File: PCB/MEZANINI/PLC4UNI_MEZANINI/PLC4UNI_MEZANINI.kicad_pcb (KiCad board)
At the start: 4 copper layers, 30.3 x 37.8 mm, 24 parts, among them U1 MC-121-L119, U2 MT9700-N

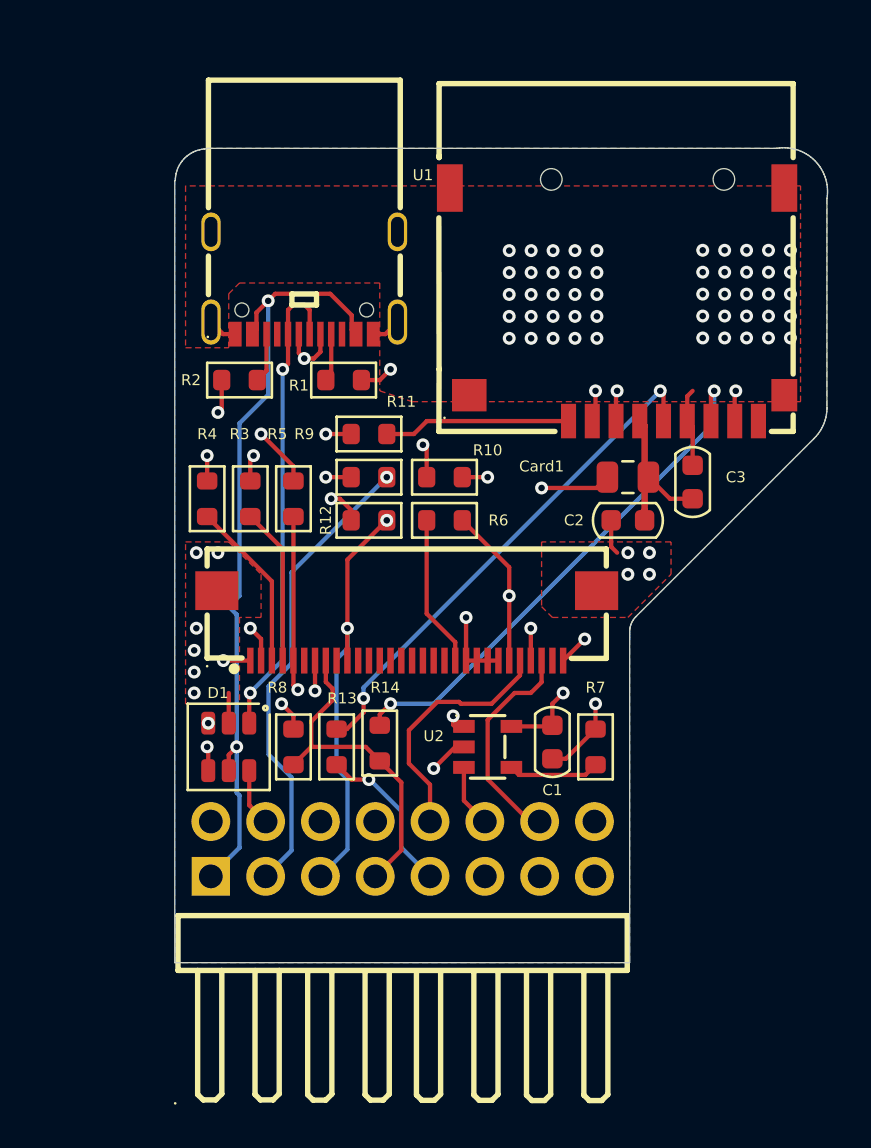
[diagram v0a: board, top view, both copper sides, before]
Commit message: ajuste de dimenciones
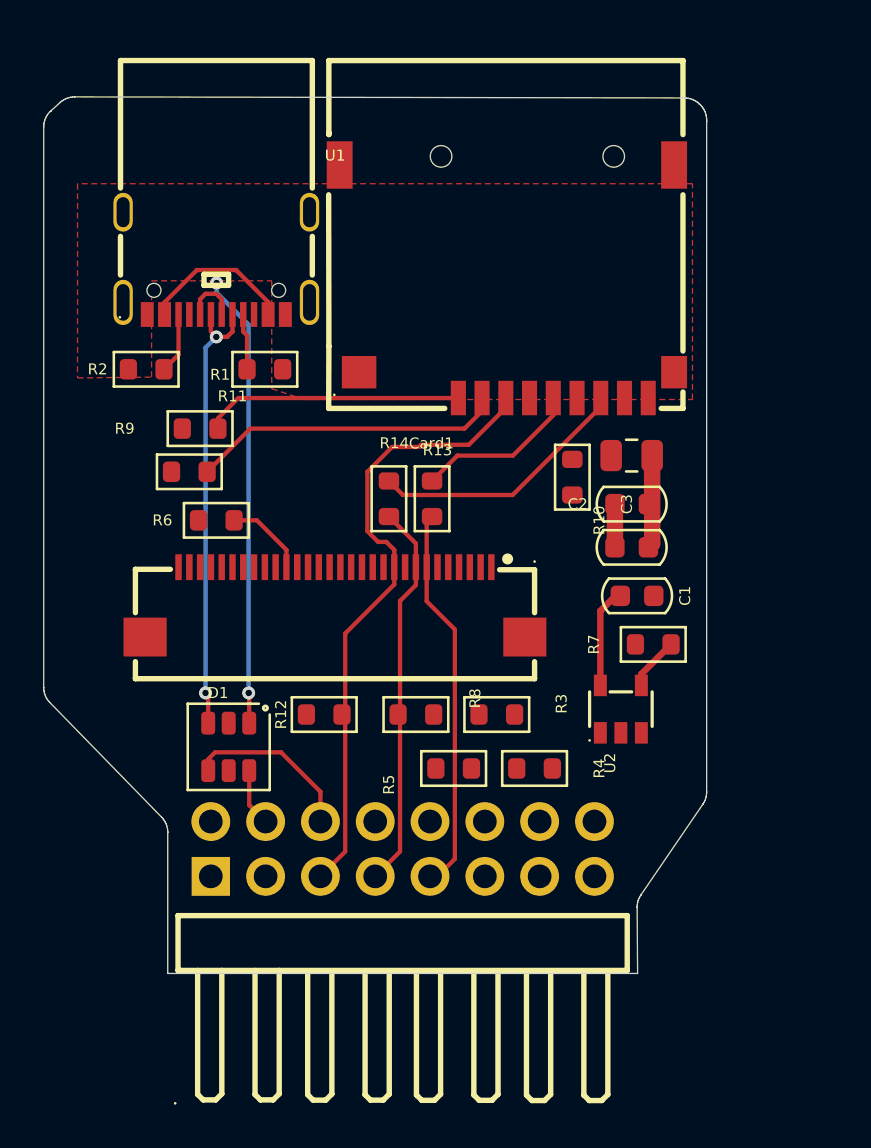
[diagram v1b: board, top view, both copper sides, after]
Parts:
- moved R4 19.7 mm to (142.1, 87.8), turned to 180 degrees
- moved R3 15.2 mm to (140.3, 85.3), turned to 180 degrees
- moved R5 14.5 mm to (138.3, 87.8), turned to 0 degrees
- moved R13 12.3 mm to (137.3, 75.3)
- moved R14 11.3 mm to (135.3, 75.3)
- moved R6 10.6 mm to (127.3, 76.3), turned to 0 degrees
- moved R12 9.24 mm to (132.3, 85.3)
- moved R9 8.33 mm to (126.1, 74.1)
- moved C1 7.83 mm to (146.8, 79.8), turned to 0 degrees
- moved R11 7.83 mm to (126.6, 72.1)
- moved U2 6.42 mm to (146.1, 85.1), turned to 0 degrees
- moved R10 5.92 mm to (143.8, 74.3), turned to -90 degrees
- moved R8 5.87 mm to (136.6, 85.3), turned to 180 degrees
- moved R7 5.45 mm to (147.6, 82.1), turned to 0 degrees
- moved Card1 5.22 mm to (140.8, 65.3)
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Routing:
- net +5V: track 36.7 -> 7.17 mm, vias 2 -> 0
- net VCC: track 29.3 -> 0.00 mm, vias 3 -> 0
- net /RESET: track 23.2 -> 0.00 mm, vias 1 -> 0
- net GND: track 24.0 -> 2.00 mm, vias 67 -> 0
- net /SD_CS: track 34.9 -> 14.5 mm, vias 2 -> 0
- net Net-(Card1-DAT1): track 16.6 -> 0.00 mm, vias 2 -> 0
- net Net-(Card1-CLK): track 23.6 -> 7.68 mm, vias 2 -> 0
- net +3.3V: track 19.0 -> 4.66 mm, vias 10 -> 0
- net /I2C_SDA: track 14.2 -> 0.00 mm, vias 1 -> 0
- net Net-(Card1-DAT0): track 24.6 -> 12.2 mm, vias 2 -> 0
- net /I2C_SCK: track 11.6 -> 0.00 mm
- net /TP_INT: track 10.2 -> 0.00 mm
- net /IM2: track 7.92 -> 0.00 mm
- net /IM1: track 7.30 -> 0.00 mm
- net /SPI_MOSI: track 34.5 -> 29.0 mm, vias 3 -> 0
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- removed copper zone on In1.Cu, net +3.3V
- removed copper zone on B.Cu, net GND
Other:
- board size 30.3 x 37.8 mm -> 30.7 x 40.6 mm
- copper layers 4 -> 2

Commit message: ensamblado en proceso
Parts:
- moved R12 9.80 mm to (133.3, 75.6)
- moved R10 2.24 mm to (142.8, 76.3), turned to 90 degrees
- moved R13 1.77 mm to (139.1, 75.1)
- moved R14 1.03 mm to (136.3, 75.1)
- moved R6 0.75 mm to (128.1, 76.3)
- moved Card1 0.68 mm to (140.8, 64.6)
- moved U1 0.59 mm to (127.3, 63.8)
- moved C1 0.35 mm to (146.6, 80.1)
- moved C2 0.25 mm to (146.6, 75.8)
- moved C3 0.25 mm to (146.6, 77.8)
- moved L1 0.25 mm to (146.6, 73.6)
- moved R11 0.25 mm to (126.3, 72.1)
- moved R2 0.25 mm to (124.3, 69.3)
- moved R7 0.25 mm to (147.6, 82.3)
- moved R9 0.25 mm to (126.3, 74.1)
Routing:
- net +3.3V: track 4.66 -> 64.3 mm, vias 0 -> 9
- net +5V: track 7.17 -> 43.1 mm
- net VCC: track 0.00 -> 29.0 mm, vias 0 -> 2
- net /TP_INT: track 0.00 -> 22.3 mm, vias 0 -> 1
- net /SD_CS: track 14.5 -> 34.7 mm, vias 0 -> 1
- net GND: track 2.00 -> 21.8 mm, vias 0 -> 51
- net /I2C_SCK: track 0.00 -> 16.6 mm, vias 0 -> 1
- net /RESET: track 0.00 -> 16.0 mm
- net /I2C_SDA: track 0.00 -> 15.2 mm, vias 0 -> 1
- net /LCD_EN: track 0.00 -> 12.5 mm, vias 0 -> 1
- net Net-(Card1-VDD): track 4.32 -> 14.6 mm, vias 0 -> 2
- net /IM2: track 0.00 -> 10.2 mm
- net /IM1: track 0.00 -> 7.21 mm
- net Net-(Card1-DAT1): track 0.00 -> 6.94 mm
- net Net-(U1-DN1): track 20.9 -> 22.6 mm
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- added copper zone on B.Cu, net GND
